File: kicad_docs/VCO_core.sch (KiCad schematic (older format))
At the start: 26 parts, among them U1 SSI2130

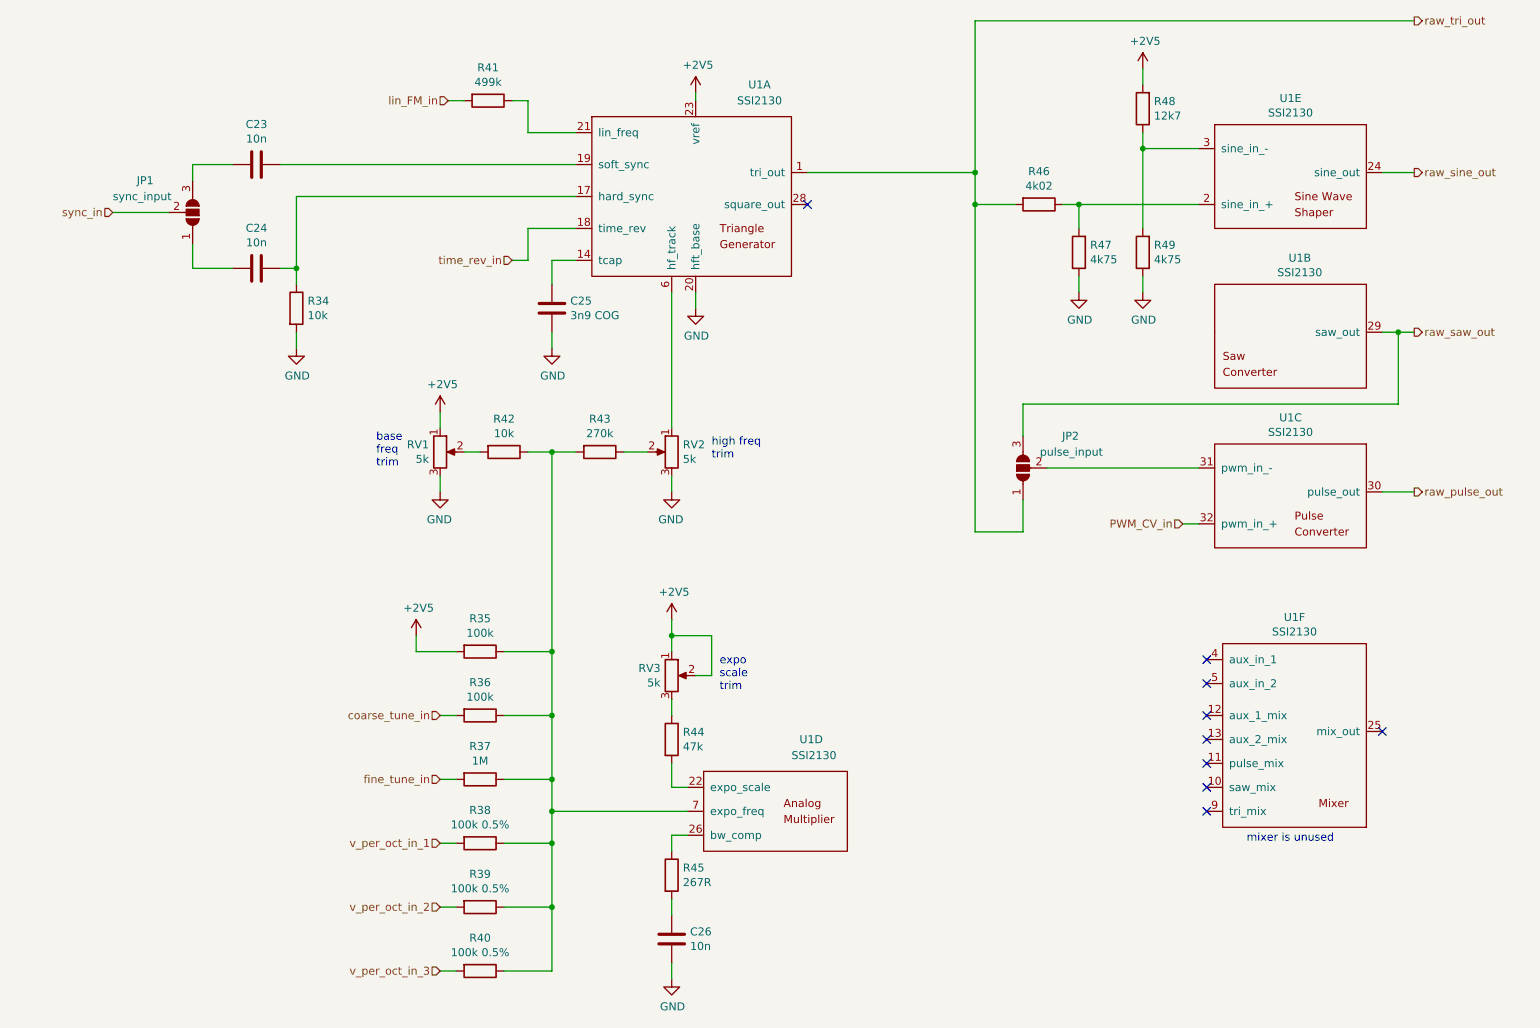
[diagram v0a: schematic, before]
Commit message: reduce amt of weird resistor vals
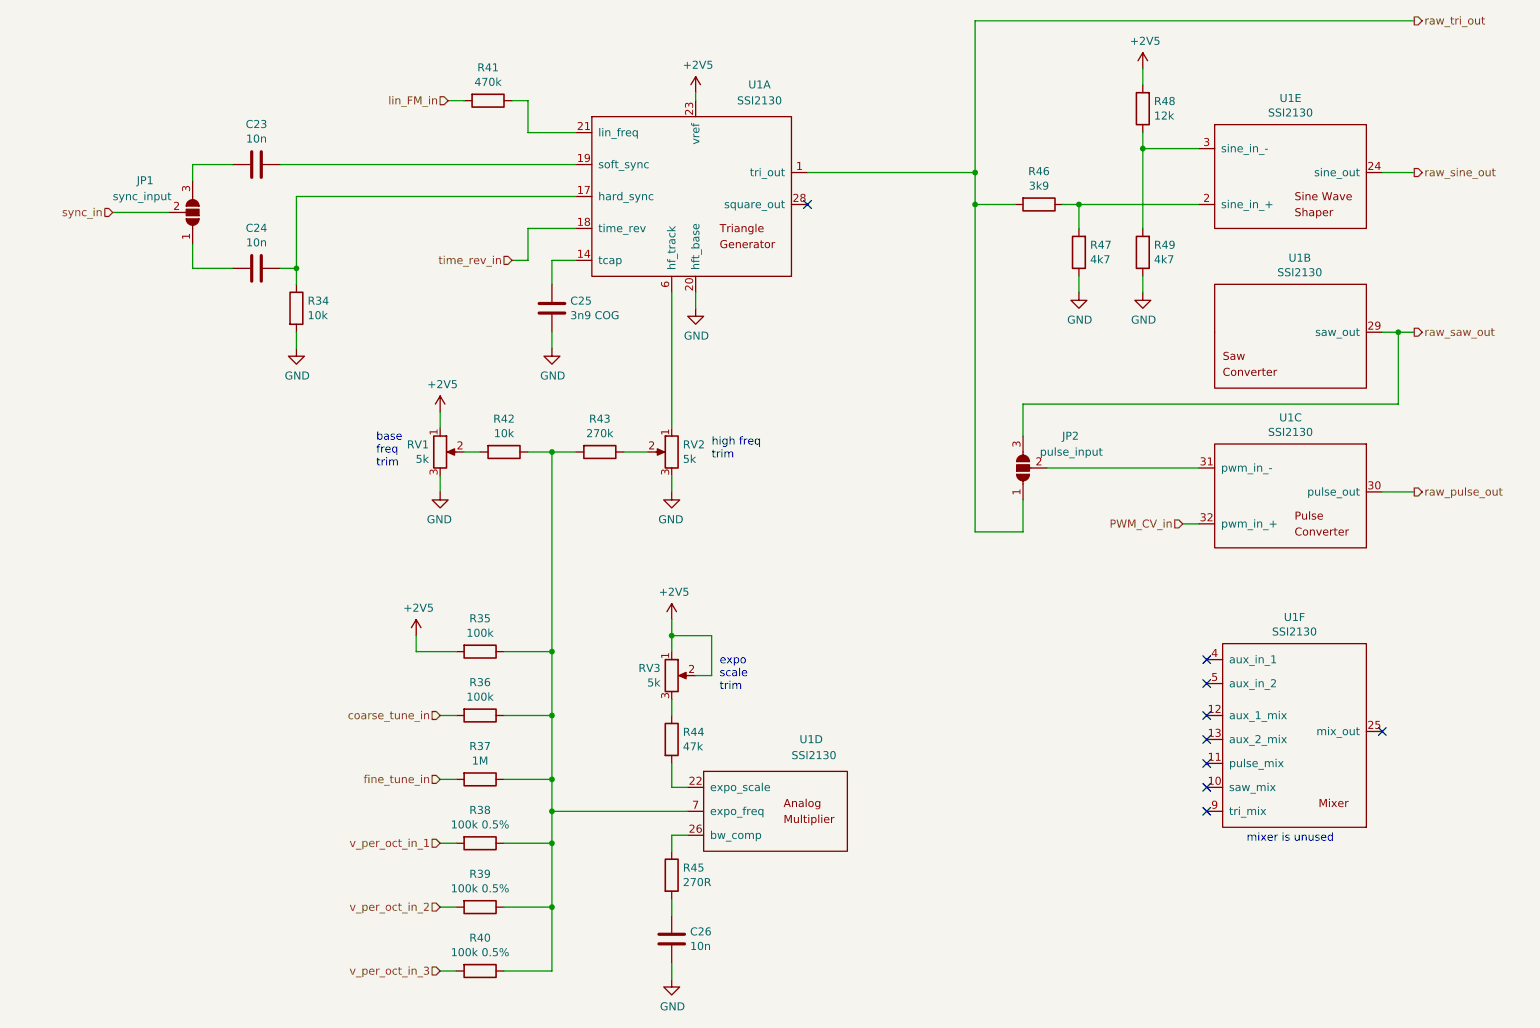
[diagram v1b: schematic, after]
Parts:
- R41: value 499k -> 470k
- R45: value 267R -> 270R
- R46: value 4k02 -> 3k9
- R47, R49: value 4k75 -> 4k7
- R48: value 12k7 -> 12k
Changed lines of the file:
@@
 $Descr A4 11693 8268
 encoding utf-8
-Sheet 6 6
+Sheet 4 6
 Title "SSI2130 VCO"
 Date "2021-12-23"
@@
 AR Path="/61D5F596/61D796C3" Ref="R45"  Part="1"
 F 0 "R45" H 4970 6546 50  0000 L CNN
-F 1 "267R" H 4970 6455 50  0000 L CNN
+F 1 "270R" H 4970 6455 50  0000 L CNN
 F 2 "Resistor_SMD:R_0805_2012Metric" V 4830 6500 50  0001 C CNN
 F 3 "~" H 4900 6500 50  0001 C CNN
@@
 AR Path="/61D5F596/61D79727" Ref="R47"  Part="1"
 F 0 "R47" H 7380 2554 50  0000 R CNN
-F 1 "4k75" H 7380 2645 50  0000 R CNN
+F 1 "4k7" H 7380 2645 50  0000 R CNN
 F 2 "Resistor_SMD:R_0805_2012Metric" V 7380 2600 50  0001 C CNN
 F 3 "~" H 7450 2600 50  0001 C CNN
@@
 AR Path="/61D5F596/61D7972D" Ref="R49"  Part="1"
 F 0 "R49" H 7780 2554 50  0000 R CNN
-F 1 "4k75" H 7780 2645 50  0000 R CNN
+F 1 "4k7" H 7780 2645 50  0000 R CNN
 F 2 "Resistor_SMD:R_0805_2012Metric" V 7780 2600 50  0001 C CNN
 F 3 "~" H 7850 2600 50  0001 C CNN
@@
 AR Path="/61D5F596/61D79740" Ref="R46"  Part="1"
 F 0 "R46" V 6993 2300 50  0000 C CNN
-F 1 "4k02" V 7084 2300 50  0000 C CNN
+F 1 "3k9" V 7084 2300 50  0000 C CNN
 F 2 "Resistor_SMD:R_0805_2012Metric" V 7130 2300 50  0001 C CNN
 F 3 "~" H 7200 2300 50  0001 C CNN
@@
 AR Path="/61D5F596/61EAEEAC" Ref="R48"  Part="1"
 F 0 "R48" H 7780 1654 50  0000 R CNN
-F 1 "12k7" H 7780 1745 50  0000 R CNN
+F 1 "12k" H 7780 1745 50  0000 R CNN
 F 2 "Resistor_SMD:R_0805_2012Metric" V 7780 1700 50  0001 C CNN
 F 3 "~" H 7850 1700 50  0001 C CNN
@@
 AR Path="/61D5F596/62248266" Ref="R41"  Part="1"
 F 0 "R41" V 3543 1650 50  0000 C CNN
-F 1 "499k" V 3634 1650 50  0000 C CNN
+F 1 "470k" V 3634 1650 50  0000 C CNN
 F 2 "Resistor_SMD:R_0805_2012Metric" V 3680 1650 50  0001 C CNN
 F 3 "~" H 3750 1650 50  0001 C CNN

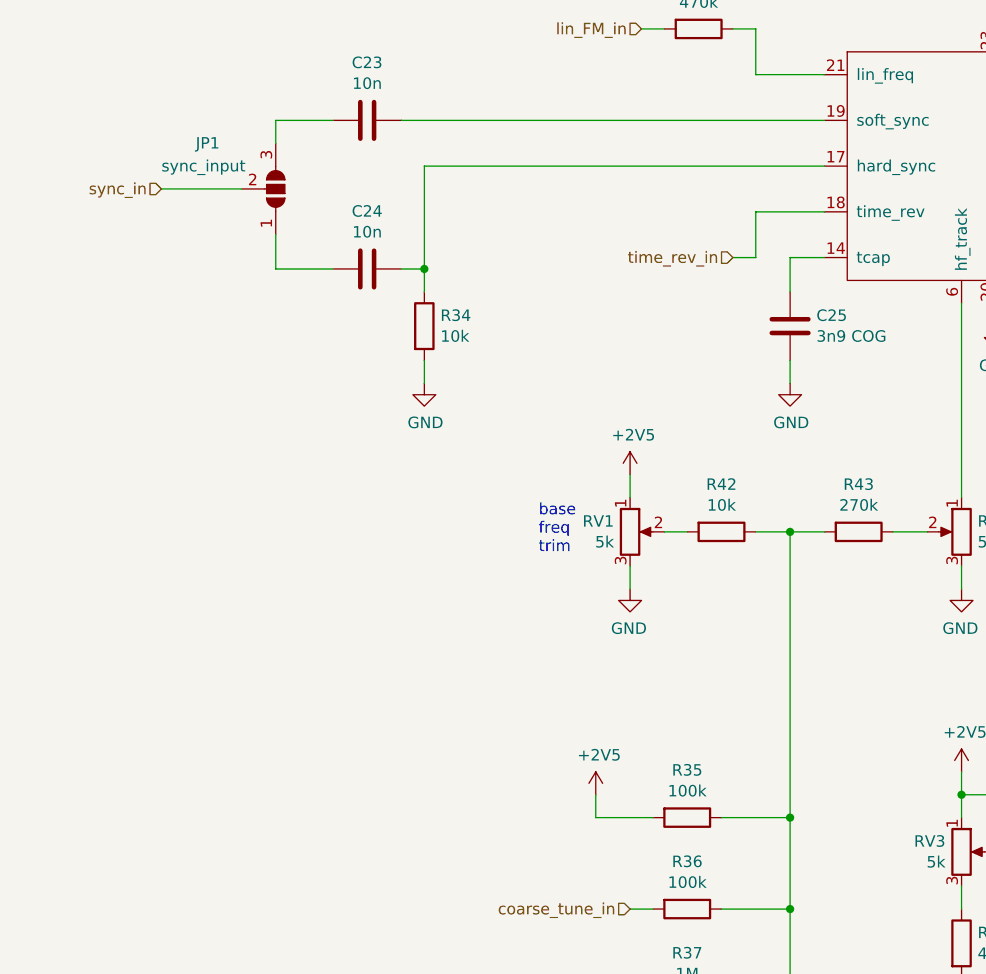
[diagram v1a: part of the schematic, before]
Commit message: add kick-start network to ensure start up
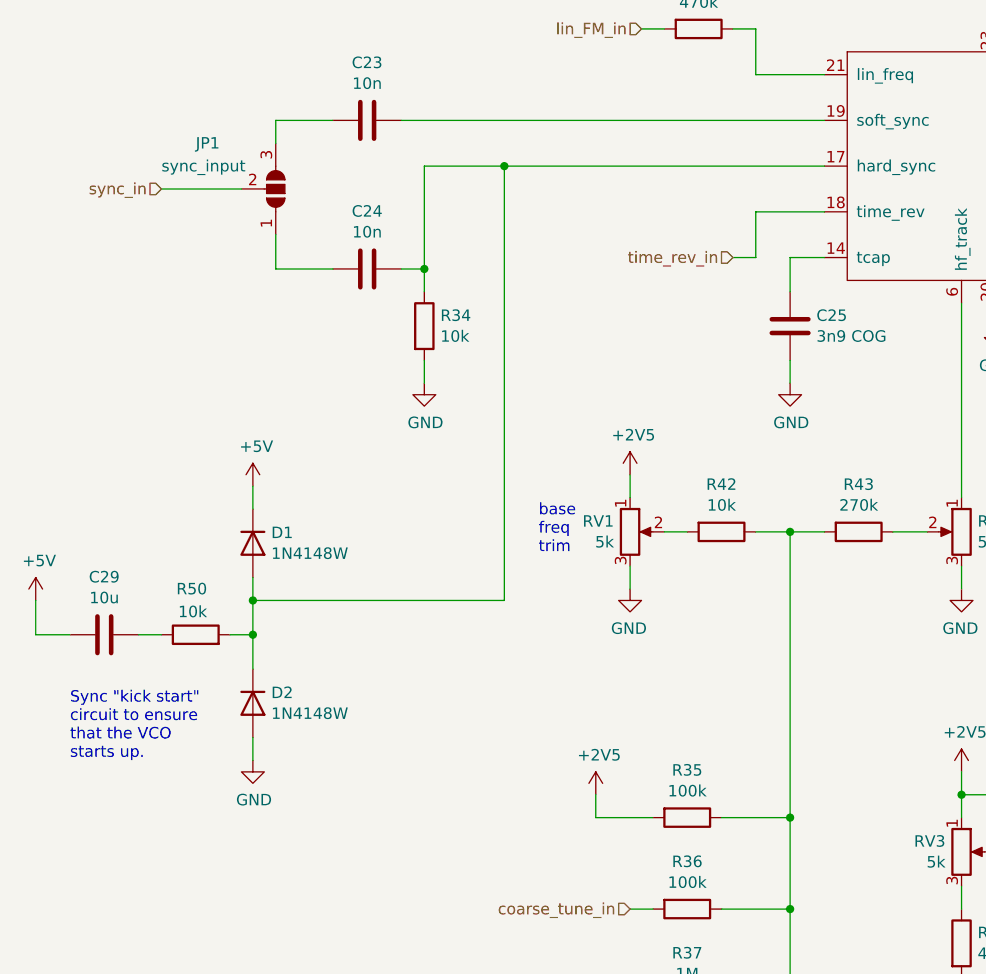
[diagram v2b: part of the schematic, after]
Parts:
- added C29: 10u, Capacitor_SMD:C_0805_2012Metric, symbol Device:C
- added D1, D2: 1N4148W, Diode_SMD:D_SOD-123, symbol Diode:1N4148W
- added R50: 10k, Resistor_SMD:R_0805_2012Metric, symbol Device:R
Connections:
- net GND: now also D2.2 (A)
- net at C24.1, R34.1, U1.17 (hard_sync): now also D1.2 (A), D2.1 (K), R50.2
- new net: C29.1, R50.1
- new net +5V: C29.2, D1.1 (K)
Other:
- note added: "Sync "kick start" \ncircuit to ensure \nthat the VCO\nstarts up."
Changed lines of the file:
@@
 	2550 2250 2550 2700
 Wire Wire Line
-	4300 2250 2550 2250
+	4300 2250 2900 2250
 Wire Wire Line
 	2550 3200 2550 3100
@@
 	4150 3850 4150 5100
 NoConn ~ 5750 2300
+Wire Wire Line
+	1800 4850 1800 4750
+$Comp
+L power:GND #PWR?
+U 1 1 61C66CF1
+P 1800 4850
+AR Path="/61C66CF1" Ref="#PWR?"  Part="1"
+AR Path="/61D5F596/61C66CF1" Ref="#PWR068"  Part="1"
+F 0 "#PWR068" H 1800 4600 50  0001 C CNN
+F 1 "GND" H 1805 4677 50  0000 C CNN
+F 2 "" H 1800 4850 50  0001 C CNN
+F 3 "" H 1800 4850 50  0001 C CNN
+	1    1800 4850
+	1    0    0    -1
+$EndComp
+Wire Wire Line
+	1400 4300 1300 4300
+$Comp
+L Device:R R?
+U 1 1 61C66CF9
+P 1550 4300
+AR Path="/61C66CF9" Ref="R?"  Part="1"
+AR Path="/61D5F596/61C66CF9" Ref="R50"  Part="1"
+F 0 "R50" V 1750 4250 50  0000 L CNN
+F 1 "10k" V 1650 4250 50  0000 L CNN
+F 2 "Resistor_SMD:R_0805_2012Metric" V 1480 4300 50  0001 C CNN
+F 3 "~" H 1550 4300 50  0001 C CNN
+	1    1550 4300
+	0    -1   -1   0
+$EndComp
+$Comp
+L Device:C C?
+U 1 1 61C66CFF
+P 1150 4300
+AR Path="/61C66CFF" Ref="C?"  Part="1"
+AR Path="/61D5F596/61C66CFF" Ref="C29"  Part="1"
+F 0 "C29" V 898 4300 50  0000 C CNN
+F 1 "10u" V 989 4300 50  0000 C CNN
+F 2 "Capacitor_SMD:C_0805_2012Metric" H 1188 4150 50  0001 C CNN
+F 3 "~" H 1150 4300 50  0001 C CNN
+	1    1150 4300
+	0    1    1    0
+$EndComp
+$Comp
+L Diode:1N4148W D1
+U 1 1 61C722F7
+P 1800 3900
+F 0 "D1" V 1754 3980 50  0000 L CNN
+F 1 "1N4148W" V 1845 3980 50  0000 L CNN
+F 2 "Diode_SMD:D_SOD-123" H 1800 3725 50  0001 C CNN
+F 3 "https://www.vishay.com/docs/85748/1n4148w.pdf" H 1800 3900 50  0001 C CNN
+	1    1800 3900
+	0    1    1    0
+$EndComp
+$Comp
+L Diode:1N4148W D2
+U 1 1 61C72C8F
+P 1800 4600
+F 0 "D2" V 1754 4680 50  0000 L CNN
+F 1 "1N4148W" V 1845 4680 50  0000 L CNN
+F 2 "Diode_SMD:D_SOD-123" H 1800 4425 50  0001 C CNN
+F 3 "https://www.vishay.com/docs/85748/1n4148w.pdf" H 1800 4600 50  0001 C CNN
+	1    1800 4600
+	0    1    1    0
+$EndComp
+Wire Wire Line
+	1800 4450 1800 4300
+Wire Wire Line
+	1700 4300 1800 4300
+Connection ~ 1800 4300
+Wire Wire Line
+	1800 4300 1800 4150
+$Comp
+L power:+5V #PWR027
+U 1 1 61C8EF04
+P 850 4150
+F 0 "#PWR027" H 850 4000 50  0001 C CNN
+F 1 "+5V" H 865 4323 50  0000 C CNN
+F 2 "" H 850 4150 50  0001 C CNN
+F 3 "" H 850 4150 50  0001 C CNN
+	1    850  4150
+	1    0    0    -1
+$EndComp
+$Comp
+L power:+5V #PWR067
+U 1 1 61C8F814
+P 1800 3650
+F 0 "#PWR067" H 1800 3500 50  0001 C CNN
+F 1 "+5V" H 1815 3823 50  0000 C CNN
+F 2 "" H 1800 3650 50  0001 C CNN
+F 3 "" H 1800 3650 50  0001 C CNN
+	1    1800 3650
+	1    0    0    -1
+$EndComp
+Wire Wire Line
+	1800 3650 1800 3750
+Wire Wire Line
+	1000 4300 850  4300
+Wire Wire Line
+	850  4300 850  4150
+Wire Wire Line
+	1800 4150 2900 4150
+Wire Wire Line
+	2900 4150 2900 2250
+Connection ~ 1800 4150
+Wire Wire Line
+	1800 4150 1800 4050
+Connection ~ 2900 2250
+Wire Wire Line
+	2900 2250 2550 2250
+Text Notes 1000 4850 0    50   ~ 0
+Sync "kick start" \ncircuit to ensure \nthat the VCO\nstarts up.
 $EndSCHEMATC
